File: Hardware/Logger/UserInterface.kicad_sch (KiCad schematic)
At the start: 24 parts, among them Q3 FDV304P, Q4 FDV304P, SW1 SW_Push, SW2 SW_Push, SW3 SW_Push, SW4 SW_Push, U2 ST7735S

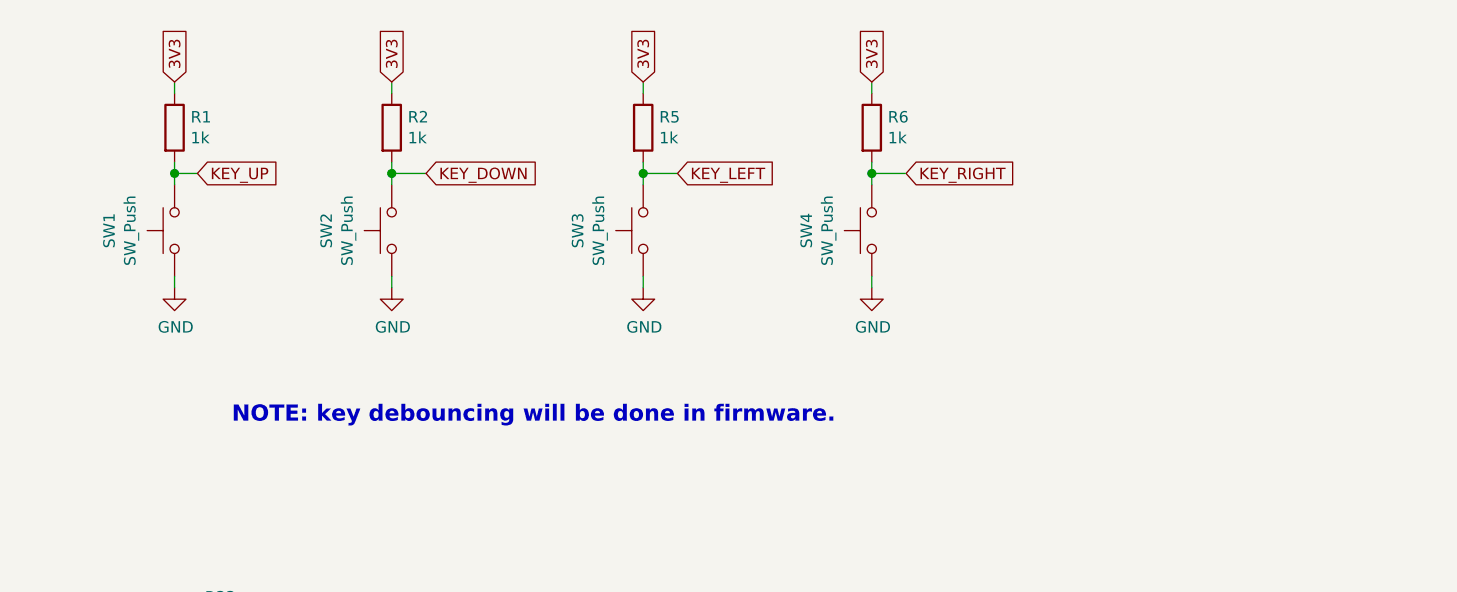
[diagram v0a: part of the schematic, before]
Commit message: 1) LCD shows data but it's malformed; 2) fix #46
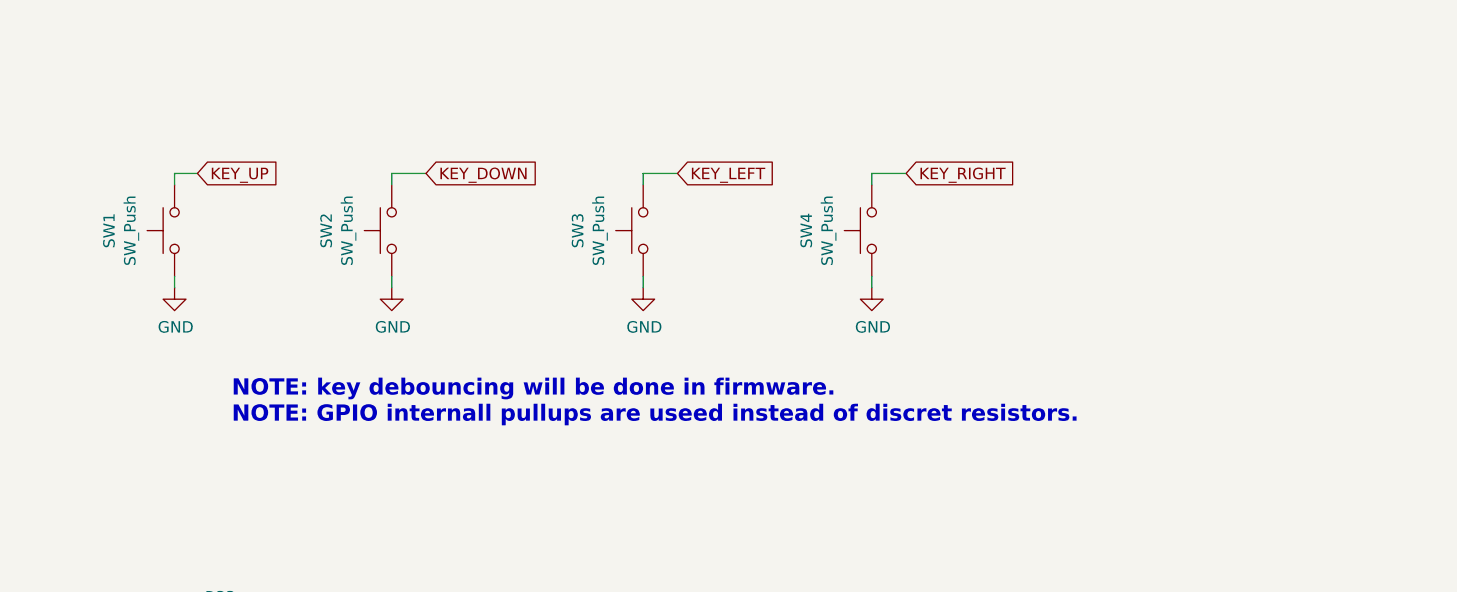
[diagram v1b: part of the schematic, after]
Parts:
- removed R1, R2, R5, R6: 1k, Resistor_SMD:R_0805_2012Metric, symbol Device:R
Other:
- note added: "NOTE: key debouncing will be done in firmware. NOTE: GPIO internall pullups are useed instead of discret resistors."
- note removed: "NOTE: key debouncing will be done in firmware."
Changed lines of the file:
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@@
 (kicad_sch (version 20210621) (generator eeschema)
   (paper "A4")
-  (junction (at 48.26 43.18) (diameter 1.016) (color 0 0 0 0))
   (junction (at 54.61 161.29) (diameter 1.016) (color 0 0 0 0))
   (junction (at 62.23 161.29) (diameter 1.016) (color 0 0 0 0))
-  (junction (at 72.39 43.18) (diameter 1.016) (color 0 0 0 0))
   (junction (at 72.39 170.18) (diameter 1.016) (color 0 0 0 0))
   (junction (at 82.55 161.29) (diameter 1.016) (color 0 0 0 0))
   (junction (at 82.55 177.8) (diameter 1.016) (color 0 0 0 0))
-  (junction (at 100.33 43.18) (diameter 1.016) (color 0 0 0 0))
   (junction (at 100.33 161.29) (diameter 1.016) (color 0 0 0 0))
   (junction (at 115.57 161.29) (diameter 1.016) (color 0 0 0 0))
-  (junction (at 125.73 43.18) (diameter 1.016) (color 0 0 0 0))
   (junction (at 196.85 113.03) (diameter 1.016) (color 0 0 0 0))
   (wire (pts (xy 44.45 95.25) (xy 49.53 95.25))
@@
     (stroke (width 0) (type solid) (color 0 0 0 0))
   )
-  (wire (pts (xy 48.26 33.02) (xy 48.26 34.29))
-    (stroke (width 0) (type solid) (color 0 0 0 0))
-  )
-  (wire (pts (xy 48.26 41.91) (xy 48.26 43.18))
-    (stroke (width 0) (type solid) (color 0 0 0 0))
-  )
   (wire (pts (xy 48.26 43.18) (xy 48.26 44.45))
     (stroke (width 0) (type solid) (color 0 0 0 0))
@@
     (stroke (width 0) (type solid) (color 0 0 0 0))
   )
-  (wire (pts (xy 72.39 33.02) (xy 72.39 34.29))
-    (stroke (width 0) (type solid) (color 0 0 0 0))
-  )
-  (wire (pts (xy 72.39 41.91) (xy 72.39 43.18))
-    (stroke (width 0) (type solid) (color 0 0 0 0))
-  )
   (wire (pts (xy 72.39 43.18) (xy 72.39 44.45))
     (stroke (width 0) (type solid) (color 0 0 0 0))
@@
     (stroke (width 0) (type solid) (color 0 0 0 0))
   )
-  (wire (pts (xy 100.33 33.02) (xy 100.33 34.29))
-    (stroke (width 0) (type solid) (color 0 0 0 0))
-  )
-  (wire (pts (xy 100.33 41.91) (xy 100.33 43.18))
-    (stroke (width 0) (type solid) (color 0 0 0 0))
-  )
   (wire (pts (xy 100.33 43.18) (xy 100.33 44.45))
     (stroke (width 0) (type solid) (color 0 0 0 0))
@@
   )
   (wire (pts (xy 115.57 189.23) (xy 115.57 181.61))
-    (stroke (width 0) (type solid) (color 0 0 0 0))
-  )
-  (wire (pts (xy 125.73 33.02) (xy 125.73 34.29))
-    (stroke (width 0) (type solid) (color 0 0 0 0))
-  )
-  (wire (pts (xy 125.73 41.91) (xy 125.73 43.18))
     (stroke (width 0) (type solid) (color 0 0 0 0))
   )
@@
     (effects (font (size 1.8034 1.8034) (thickness 0.3607) bold) (justify left bottom))
   )
-  (text "NOTE: key debouncing will be done in firmware." (at 54.61 71.12 0)
+  (text "NOTE: key debouncing will be done in firmware.\nNOTE: GPIO internall pullups are useed instead of discret resistors."
+    (at 54.61 71.12 0)
     (effects (font (size 1.8034 1.8034) (thickness 0.3607) bold) (justify left bottom))
   )
@@
     )
   )
-  (global_label "3V3" (shape input) (at 48.26 33.02 90) (fields_autoplaced)
-    (effects (font (size 1.27 1.27)) (justify left))
-    (property "Intersheet References" "${INTERSHEET_REFS}" (id 0) (at -97.79 -45.72 0)
-      (effects (font (size 1.27 1.27)) hide)
-    )
-  )
   (global_label "LCD_BRIGHT_PWM" (shape input) (at 48.26 170.18 180) (fields_autoplaced)
     (effects (font (size 1.27 1.27)) (justify right))
@@
     )
   )
-  (global_label "3V3" (shape input) (at 72.39 33.02 90) (fields_autoplaced)
-    (effects (font (size 1.27 1.27)) (justify left))
-    (property "Intersheet References" "${INTERSHEET_REFS}" (id 0) (at -73.66 -45.72 0)
-      (effects (font (size 1.27 1.27)) hide)
-    )
-  )
   (global_label "3V3" (shape input) (at 72.39 97.79 90) (fields_autoplaced)
     (effects (font (size 1.27 1.27)) (justify left))
@@
     )
   )
-  (global_label "3V3" (shape input) (at 100.33 33.02 90) (fields_autoplaced)
-    (effects (font (size 1.27 1.27)) (justify left))
-    (property "Intersheet References" "${INTERSHEET_REFS}" (id 0) (at -45.72 -45.72 0)
-      (effects (font (size 1.27 1.27)) hide)
-    )
-  )
   (global_label "KEY_LEFT" (shape input) (at 104.14 43.18 0) (fields_autoplaced)
     (effects (font (size 1.27 1.27)) (justify left))
     (property "Intersheet References" "${INTERSHEET_REFS}" (id 0) (at 0 0 0)
-      (effects (font (size 1.27 1.27)) hide)
-    )
-  )
-  (global_label "3V3" (shape input) (at 125.73 33.02 90) (fields_autoplaced)
-    (effects (font (size 1.27 1.27)) (justify left))
-    (property "Intersheet References" "${INTERSHEET_REFS}" (id 0) (at -20.32 -45.72 0)
       (effects (font (size 1.27 1.27)) hide)
     )
@@
     )
     (pin "1")
-  )
-  (symbol (lib_id "Device:R") (at 48.26 38.1 0) (unit 1)
-    (in_bom yes) (on_board yes)
-    (property "Reference" "R1" (id 0) (at 50.038 36.9316 0)
-      (effects (font (size 1.27 1.27)) (justify left))
-    )
-    (property "Value" "1k" (id 1) (at 50.038 39.243 0)
-      (effects (font (size 1.27 1.27)) (justify left))
-    )
-    (property "Footprint" "Resistor_SMD:R_0805_2012Metric" (id 2) (at 46.482 38.1 90)
-      (effects (font (size 1.27 1.27)) hide)
-    )
-    (property "Datasheet" "~" (id 3) (at 48.26 38.1 0)
-      (effects (font (size 1.27 1.27)) hide)
-    )
-    (pin "1")
-    (pin "2")
   )
   (symbol (lib_id "Device:R") (at 53.34 95.25 90) (unit 1)
@@
     (pin "2")
   )
-  (symbol (lib_id "Device:R") (at 72.39 38.1 0) (unit 1)
-    (in_bom yes) (on_board yes)
-    (property "Reference" "R2" (id 0) (at 74.168 36.9316 0)
-      (effects (font (size 1.27 1.27)) (justify left))
-    )
-    (property "Value" "1k" (id 1) (at 74.168 39.243 0)
-      (effects (font (size 1.27 1.27)) (justify left))
-    )
-    (property "Footprint" "Resistor_SMD:R_0805_2012Metric" (id 2) (at 70.612 38.1 90)
-      (effects (font (size 1.27 1.27)) hide)
-    )
-    (property "Datasheet" "~" (id 3) (at 72.39 38.1 0)
-      (effects (font (size 1.27 1.27)) hide)
-    )
-    (pin "1")
-    (pin "2")
-  )
   (symbol (lib_id "Device:R") (at 72.39 180.34 0) (unit 1)
     (in_bom yes) (on_board yes)
@@
       (effects (font (size 1.27 1.27)) hide)
     )
-    (pin "1")
-    (pin "2")
-  )
-  (symbol (lib_id "Device:R") (at 100.33 38.1 0) (unit 1)
-    (in_bom yes) (on_board yes)
-    (property "Reference" "R5" (id 0) (at 102.108 36.9316 0)
-      (effects (font (size 1.27 1.27)) (justify left))
-    )
-    (property "Value" "1k" (id 1) (at 102.108 39.243 0)
-      (effects (font (size 1.27 1.27)) (justify left))
-    )
-    (property "Footprint" "Resistor_SMD:R_0805_2012Metric" (id 2) (at 98.552 38.1 90)
-      (effects (font (size 1.27 1.27)) hide)
-    )
-    (property "Datasheet" "~" (id 3) (at 100.33 38.1 0)
-      (effects (font (size 1.27 1.27)) hide)
-    )
-    (pin "1")
-    (pin "2")
-  )
-  (symbol (lib_id "Device:R") (at 125.73 38.1 0) (unit 1)
-    (in_bom yes) (on_board yes)
-    (property "Reference" "R6" (id 0) (at 127.508 36.9316 0)
-      (effects (font (size 1.27 1.27)) (justify left))
-    )
-    (property "Value" "1k" (id 1) (at 127.508 39.243 0)
-      (effects (font (size 1.27 1.27)) (justify left))
-    )
-    (property "Footprint" "Resistor_SMD:R_0805_2012Metric" (id 2) (at 123.952 38.1 90)
-      (effects (font (size 1.27 1.27)) hide)
-    )
-    (property "Datasheet" "~" (id 3) (at 125.73 38.1 0)
-      (effects (font (size 1.27 1.27)) hide)
-    )

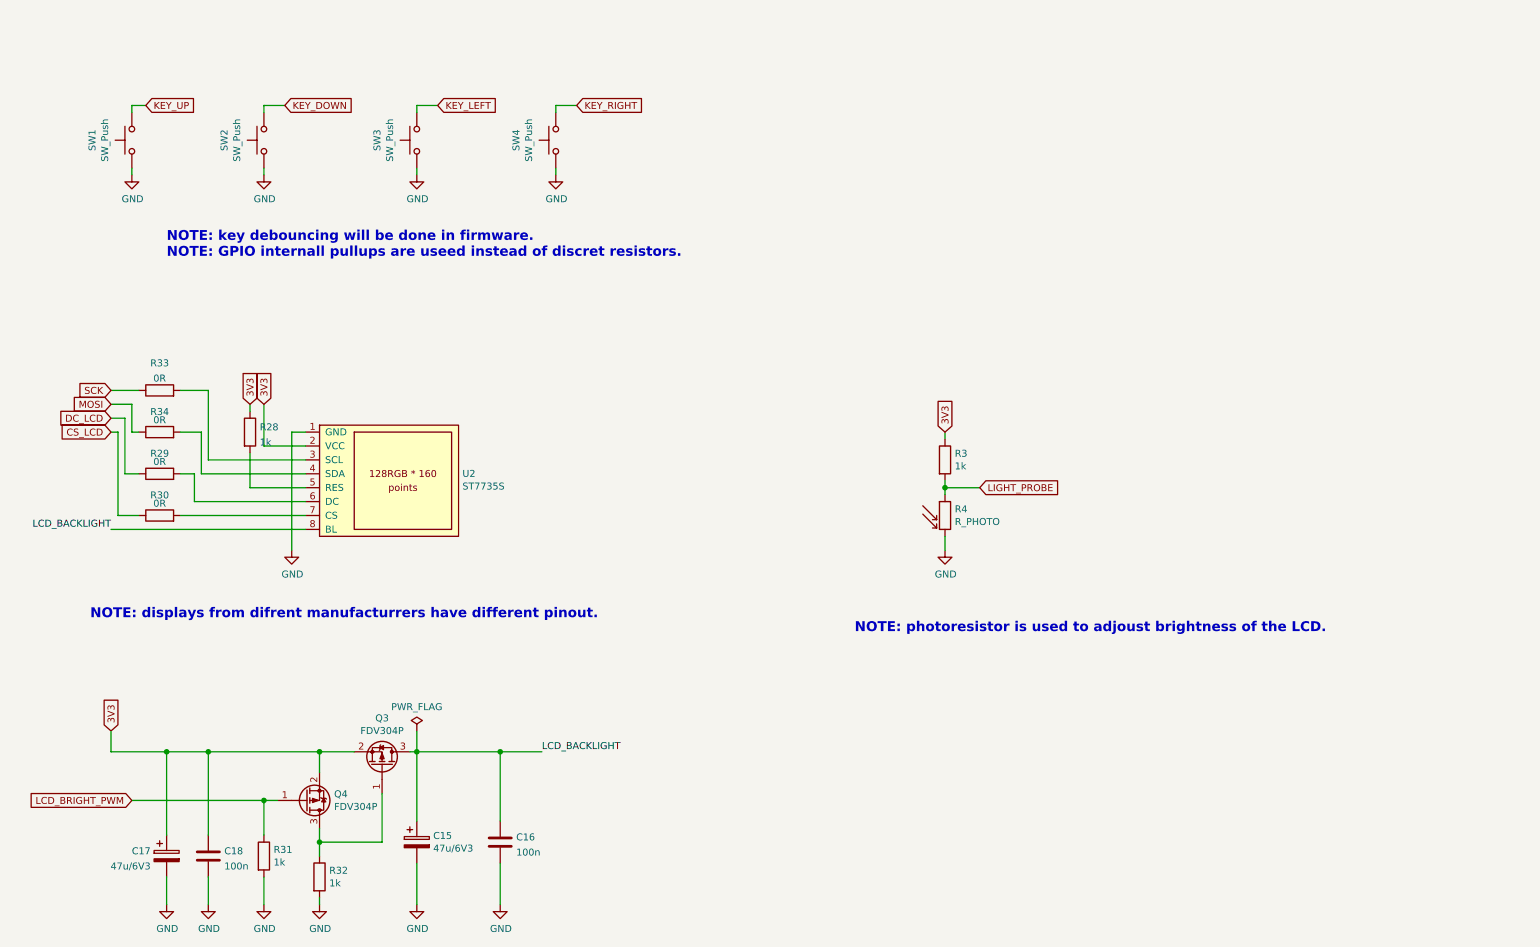
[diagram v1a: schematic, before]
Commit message: 1) LCD works ok now 2) fix #49 3) fix #50
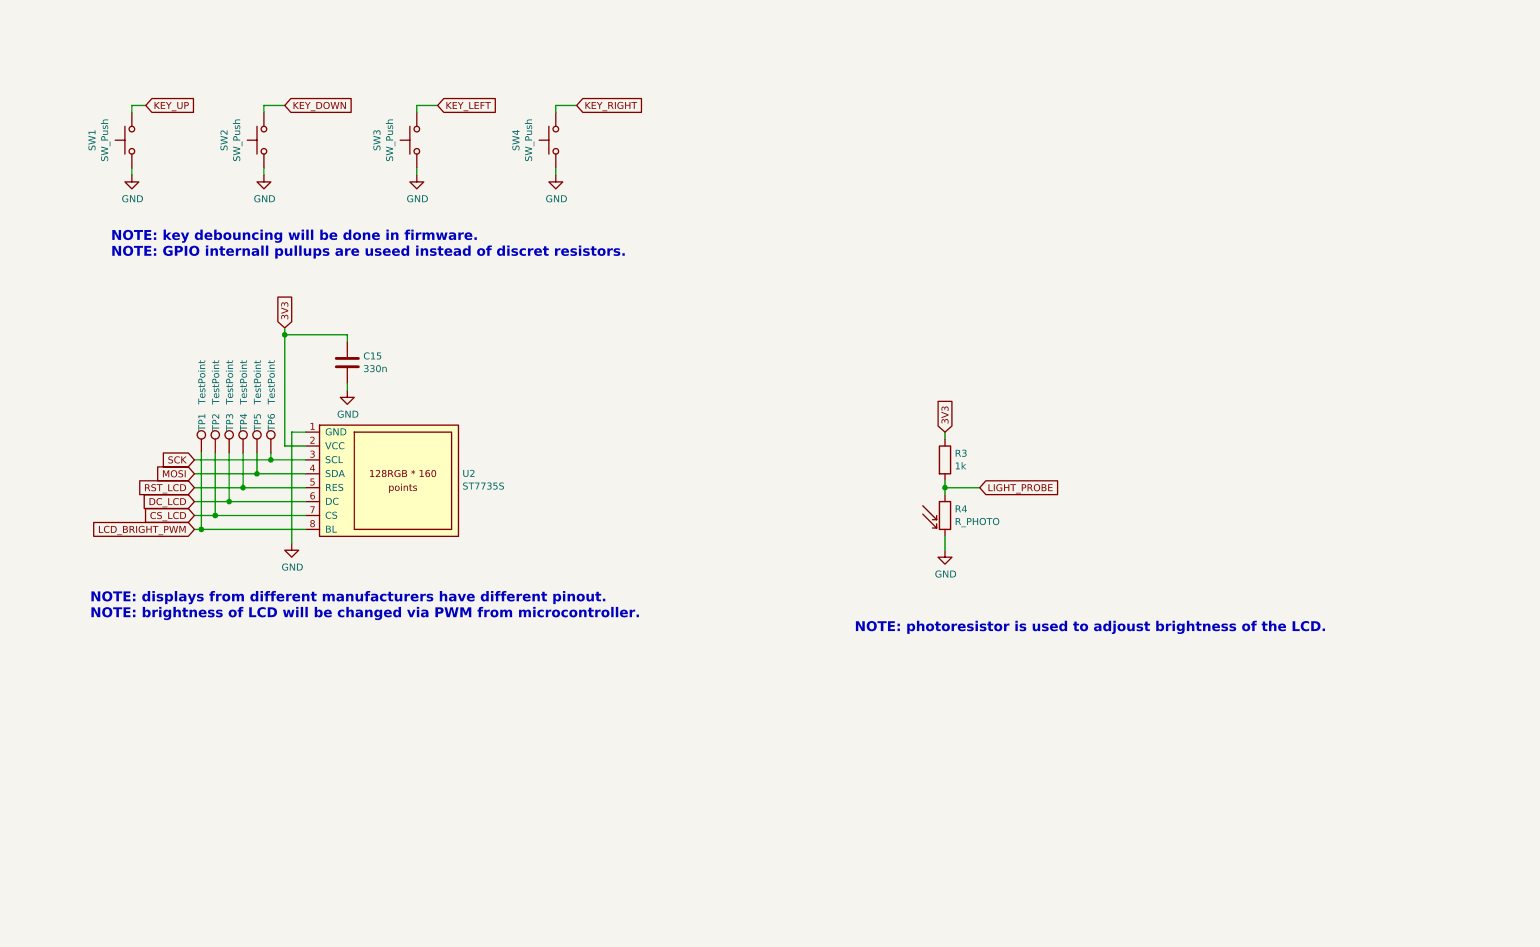
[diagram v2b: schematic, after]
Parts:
- removed C15, C17: 47u/6V3, Capacitor_Tantalum_SMD:CP_EIA-3528-21_Kemet-B, symbol Device:CP
- removed C16, C18: 100n, Capacitor_SMD:C_0805_2012Metric, symbol Device:C
- removed Q3, Q4: FDV304P, Package_TO_SOT_SMD:SOT-23, symbol Device:Q_PMOS_GSD
- removed R28, R31, R32: 1k, Resistor_SMD:R_0805_2012Metric, symbol Device:R
- removed R29, R30, R33, R34: 0R, Resistor_SMD:R_0805_2012Metric, symbol Device:R
- added C15: 330n, Capacitor_SMD:C_0805_2012Metric, symbol Device:C
- added TP1, TP2, TP3, TP4, TP5, TP6: TestPoint, TestPoint:TestPoint_Pad_D1.5mm, symbol Connector:TestPoint
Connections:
- net LCD_BACKLIGHT is gone; now on net LCD_BRIGHT_PWM: U2.8 (BL)
- net 3V3: now also C15.1
- net CS_LCD: now also U2.7 (CS), TP2.1
- net DC_LCD: now also U2.6 (DC), TP3.1
- net GND: now also C15.2
- net LCD_BRIGHT_PWM: now also TP1.1
- net MOSI: now also U2.4 (SDA), TP5.1
- net SCK: now also U2.3 (SCL), TP6.1
- net RST_LCD: now reaches U2.5 (RES)
- net RST_LCD: now also TP4.1
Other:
- note added: "NOTE: displays from different manufacturers have different pinout. NOTE: brightness of LCD will be changed via PWM from microcontroller."
- note removed: "NOTE: displays from difrent manufacturrers have different pinout."

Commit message: fixed SPI connections to SD card, added ESD protection for SD card
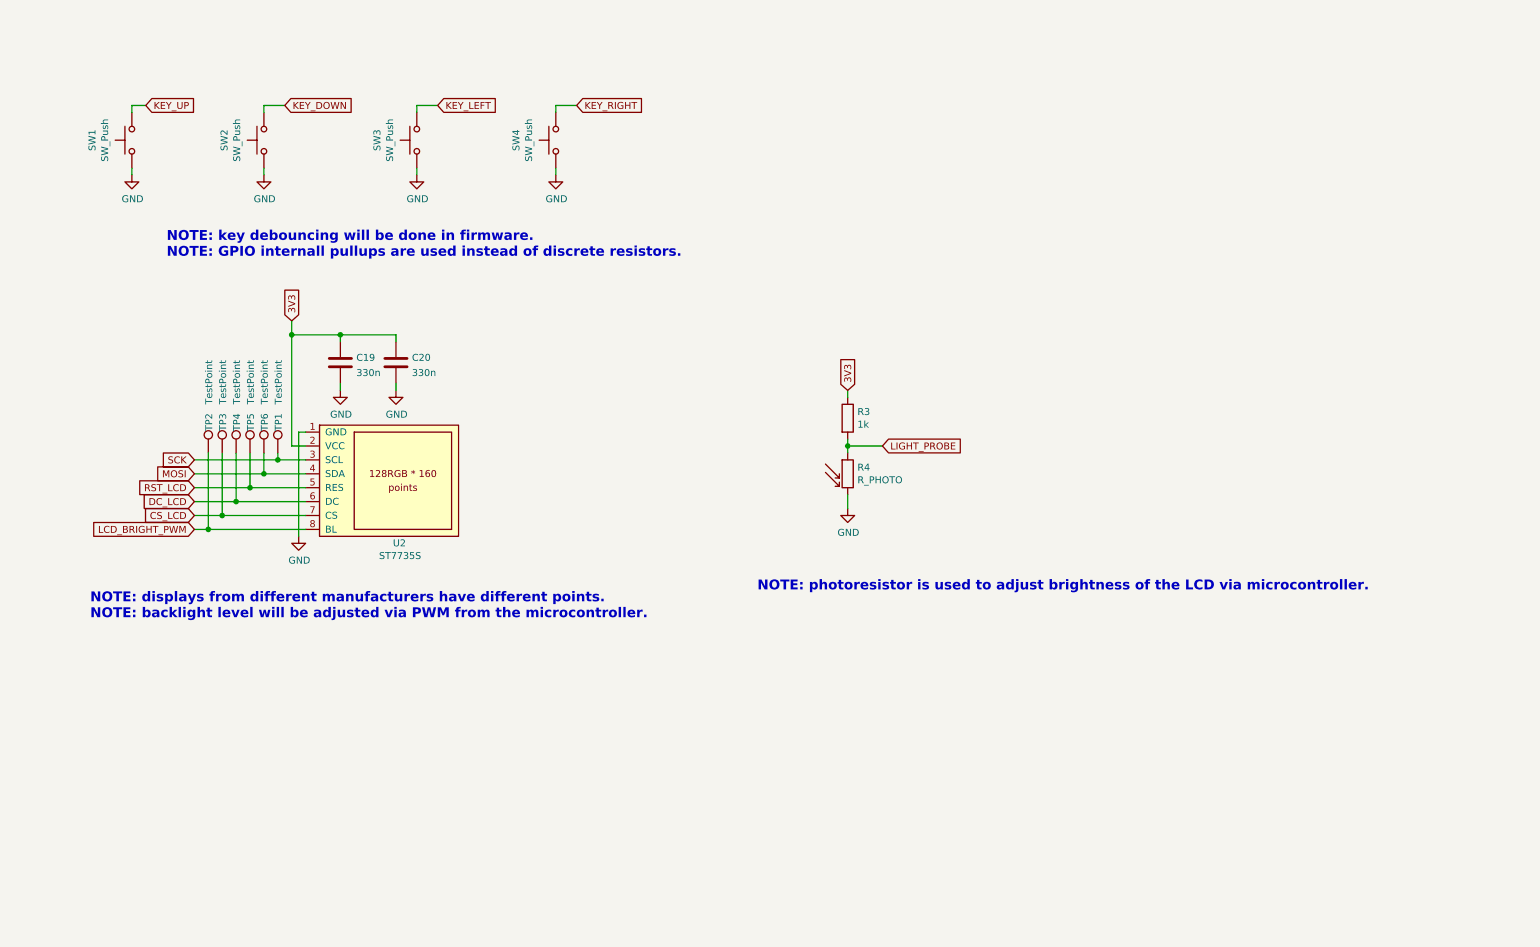
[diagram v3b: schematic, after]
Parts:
- removed C15: 330n, Capacitor_SMD:C_0805_2012Metric, symbol Device:C
- added C19, C20: 330n, Capacitor_SMD:C_0805_2012Metric, symbol Device:C
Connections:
- net 3V3: now also C19.1, C20.1
- net CS_LCD: now also TP3.1; no longer TP2.1
- net DC_LCD: now also TP4.1; no longer TP3.1
- net GND: now also C19.2, C20.2
- net LCD_BRIGHT_PWM: now also TP2.1; no longer TP1.1
- net MOSI: now also TP6.1; no longer TP5.1
- net RST_LCD: now also TP5.1; no longer TP4.1
- net SCK: now also TP1.1; no longer TP6.1
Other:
- note added: "NOTE: displays from different manufacturers have different points. NOTE: backlight level will be adjusted via PWM from the microcontroller."
- note added: "NOTE: key debouncing will be done in firmware. NOTE: GPIO internall pullups are used instead of discrete resistors."
- note added: "NOTE: photoresistor is used to adjust brightness of the LCD via microcontroller."
- note removed: "NOTE: displays from different manufacturers have different pinout. NOTE: brightness of LCD will be changed via PWM from microcontroller."
- note removed: "NOTE: key debouncing will be done in firmware. NOTE: GPIO internall pullups are useed instead of discret resistors."
- note removed: "NOTE: photoresistor is used to adjoust brightness of the LCD."
- moved on the sheet: R3, R4
